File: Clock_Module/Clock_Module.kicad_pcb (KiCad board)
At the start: 2 copper layers, 95.9 x 90.2 mm, 30 parts, among them J1 Conn_01x12, J2 Conn_01x16, SW1 Switch, U1 74LS08, U2 74LS32, U3 74LS04, U4 LM555xN, U5 LM555xN, U6 LM555xN

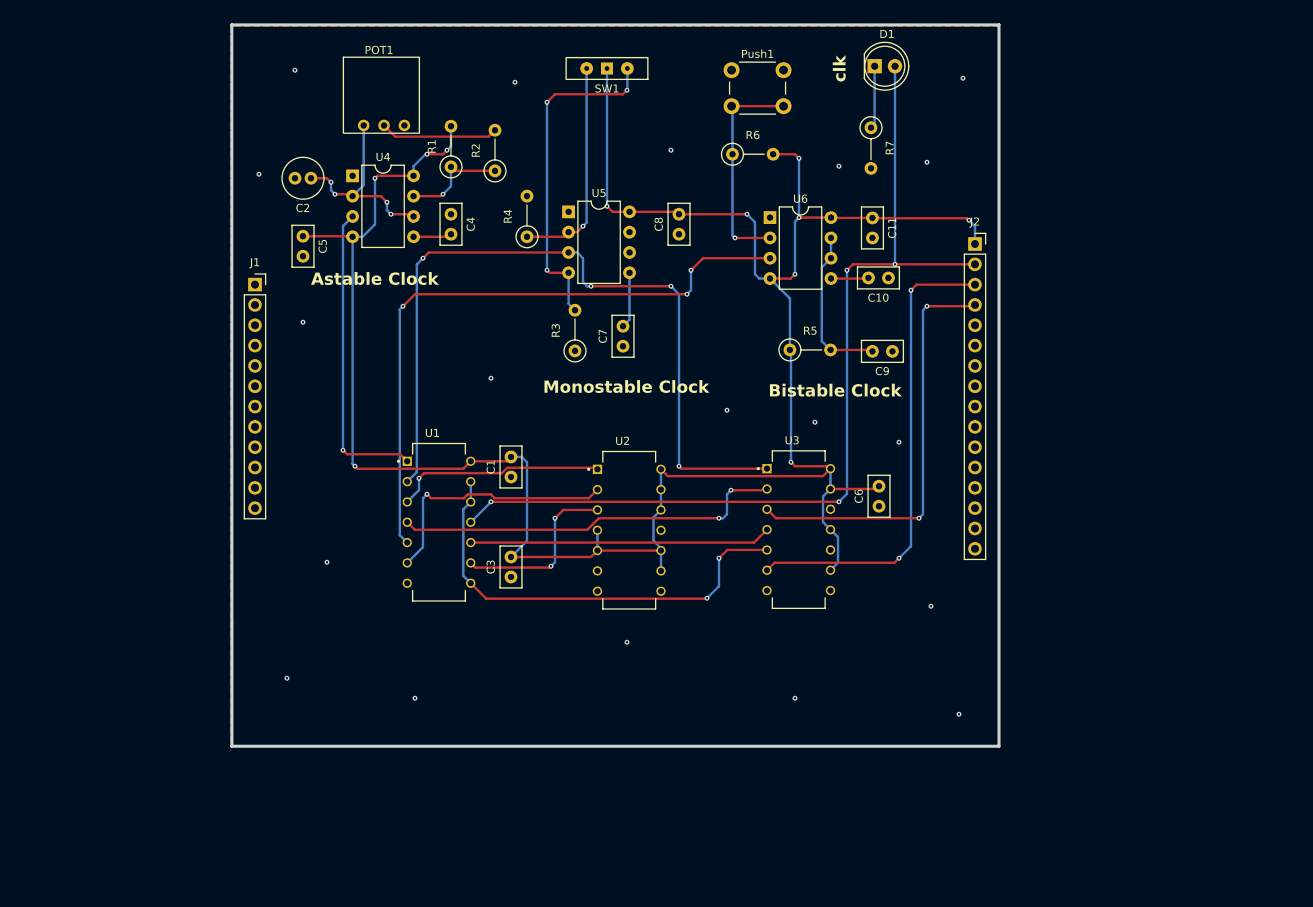
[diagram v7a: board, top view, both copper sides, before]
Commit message: fixed clock module, made it back into pc104 board standard
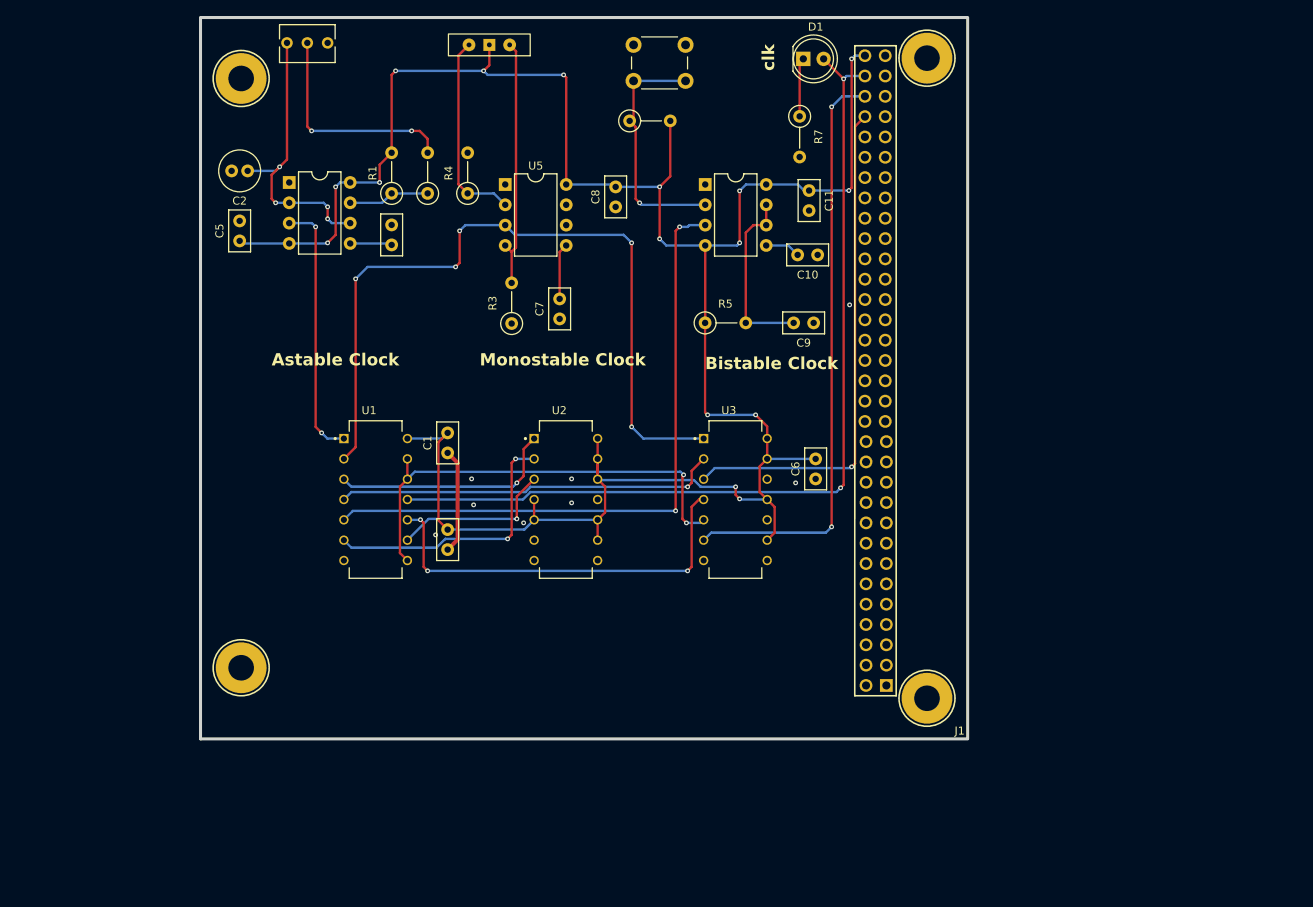
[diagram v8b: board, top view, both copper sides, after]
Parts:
- removed J2: Conn_01x16, Connector_PinSocket_2.54mm:PinSocket_1x16_P2.54mm_Vertical
- J1: value Conn_01x12 -> ~; footprint Connector_PinSocket_2.54mm:PinSocket_1x12_P2.54mm_Vertical -> MyFootPrints:PC104-Standard
- moved J1 105.6 mm to (173.9, 126.1)
- moved SW1 15.0 mm to (114.1, 39.3)
- moved R6 13.5 mm to (131.6, 48.8)
- moved Push1 12.7 mm to (132.1, 39.3)
- moved R5 11.1 mm to (141.1, 74.1)
- moved C9 10.5 mm to (154.6, 74.1)
- moved C10 9.31 mm to (155.1, 65.6)
- moved R4 9.19 mm to (111.4, 57.9)
- moved U6 9.10 mm to (141.1, 56.8)
- moved R7 9.03 mm to (152.9, 48.3)
- moved D1 8.97 mm to (153.3, 41.1)
- moved R2 8.88 mm to (106.4, 57.9)
- moved U2 8.80 mm to (123.7, 96.2)
- moved U3 8.77 mm to (144.8, 96.2)
- moved C6 8.63 mm to (154.9, 93.6)
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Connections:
- J1 pad 1: unconnected-(J1-Pin_1-Pad1) -> GND
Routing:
- net /~{CLK}: track 59.5 -> 73.9 mm
- net Net-(U1-Pad10): track 37.7 -> 51.0 mm, vias 0 -> 3
- net GND: track 0.00 -> 13.1 mm, vias 19 -> 8
- net Net-(POT1-Pad2): track 14.8 -> 27.9 mm, vias 0 -> 2
- net /halt: track 52.4 -> 63.6 mm, vias 2 -> 1
- net Net-(U4-THR): track 25.4 -> 36.5 mm
- net Net-(SW1-C): track 42.2 -> 31.4 mm, vias 3 -> 0
- net 5V: track 291.9 -> 284.7 mm, vias 11 -> 16
- net /Clock/astable_out: track 38.3 -> 32.6 mm, vias 1 -> 2
- net /CLK: track 117.5 -> 112.4 mm, vias 4 -> 2
- net Net-(U6-TR): track 27.5 -> 30.8 mm
- net Net-(U4-DIS): track 13.3 -> 10.2 mm, vias 1 -> 0
- net Net-(SW1-A): track 27.5 -> 24.9 mm, vias 1 -> 0
- net Net-(U6-DIS): track 20.2 -> 22.7 mm
- net Net-(U1-Pad3): track 26.5 -> 28.6 mm
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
